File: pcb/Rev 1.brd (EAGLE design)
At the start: 76.8 x 76.8 mm, 216 parts, among them J1 3220-10-0100-00, J2 10118194-0001LF, J3 B2B-PH-K-S(LF)(SN), Q1 MMBT3904,215MMBT3904,215, Q12 MMBT3904,215MMBT3904,215, Q13 MMBT3904,215MMBT3904,215, Q14 MMBT3904,215MMBT3904,215, Q15 MMBT3904,215MMBT3904,215, Q16 TEFT4300, Q17 TEFT4300, Q18 TEFT4300, Q19 TEFT4300, Q20 MMBT3904,215MMBT3904,215, Q21 MMBT3904,215MMBT3904,215, Q22 MMBT3904,215MMBT3904,215, Q23 MMBT3904,215MMBT3904,215, Q24 TEFT4300, Q25 TEFT4300, Q26 TEFT4300, Q27 TEFT4300, Q28 SI7157DP, Q29 SI7157DP, Q30 MMBT3906, Q31 MMBT3906, Q32 SI7157DP, Q33 MMBT3906, Q34 MMBT3906, U1 ATSAMD21G18A-MU, U10 DRV8871, U11 PCAL6416A, U12 MAX7315, U2 AP3441, U3 TPS61089, U4 BNO055, U5 MCP73811, U7 DRV8871, U8 DRV8871, U9 DRV8871

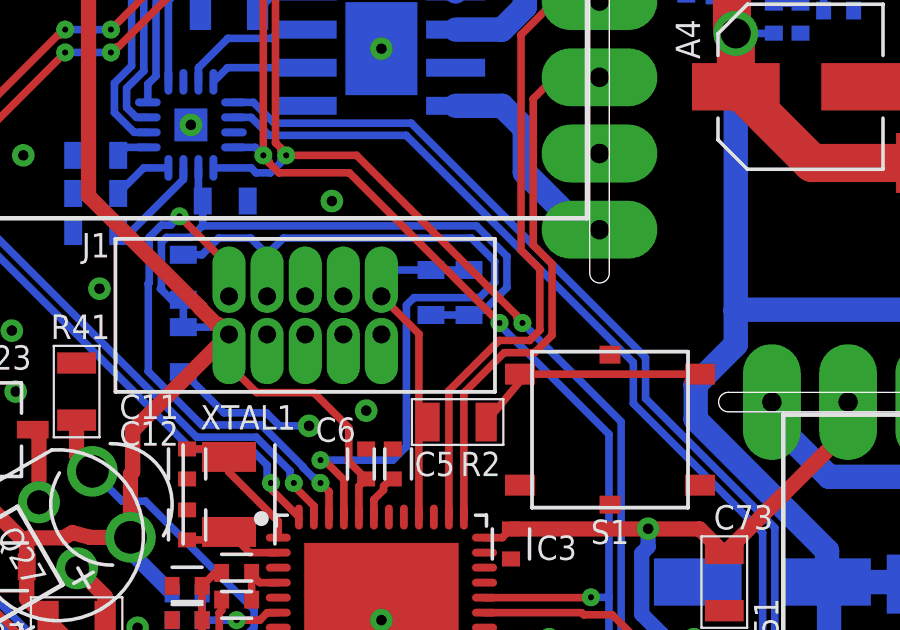
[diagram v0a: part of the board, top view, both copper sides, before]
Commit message: Fixed C7 that was somehow a resistor
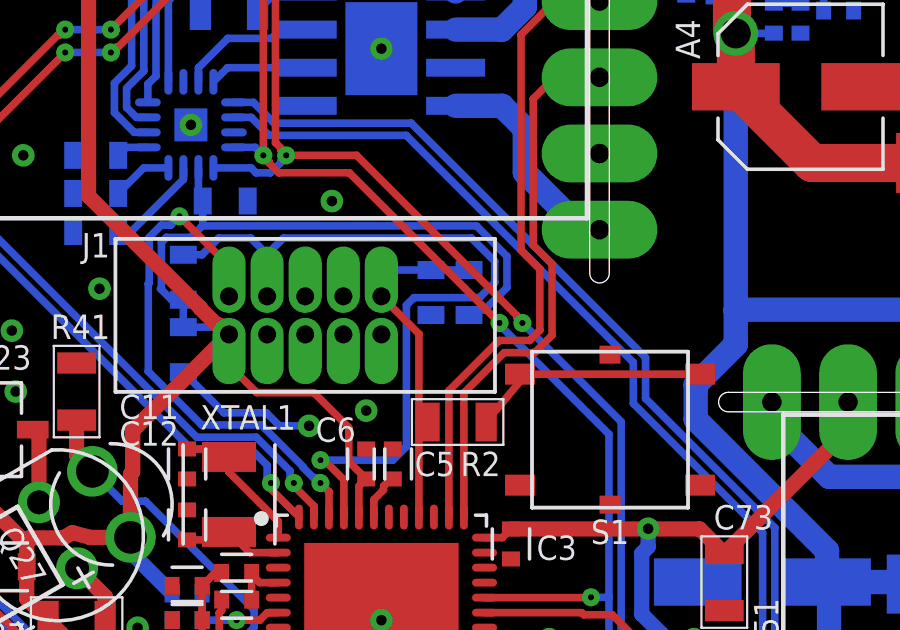
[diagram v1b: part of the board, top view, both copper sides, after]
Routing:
- net +3V3: track 499.9 -> 498.6 mm
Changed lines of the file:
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@@
 <contactref element="FB1" pad="2"/>
 <contactref element="R1" pad="2"/>
-<contactref element="C7" pad="2"/>
 <contactref element="R5" pad="2"/>
 <contactref element="J1" pad="P1"/>
@@
 <wire x1="59.944" y1="20.298" x2="59.944" y2="16.764" width="1.27" layer="16"/>
 <wire x1="59.944" y1="16.764" x2="59.69" y2="16.51" width="1.27" layer="16"/>
-<wire x1="20.701" y1="29.222" x2="21.971" y2="29.222" width="0.254" layer="16"/>
 <wire x1="12.446" y1="28.817" x2="13.728" y2="28.817" width="0.254" layer="16"/>
 <wire x1="13.728" y1="28.817" x2="13.97" y2="28.575" width="0.254" layer="16"/>
@@
 <wire x1="16.8004" y1="26.6336" x2="17.9626" y2="25.4714" width="0.254" layer="1"/>
 <wire x1="17.9626" y1="24.3364" x2="18.542" y2="23.757" width="0.254" layer="1"/>
+<contactref element="C7" pad="2"/>
+<wire x1="22.86" y1="53.492" x2="22.86" y2="55.88" width="0" layer="19" extent="1-1"/>
+<wire x1="20.701" y1="29.222" x2="21.971" y2="29.222" width="0" layer="19" extent="16-16"/>
 </signal>
 <signal name="N$7">

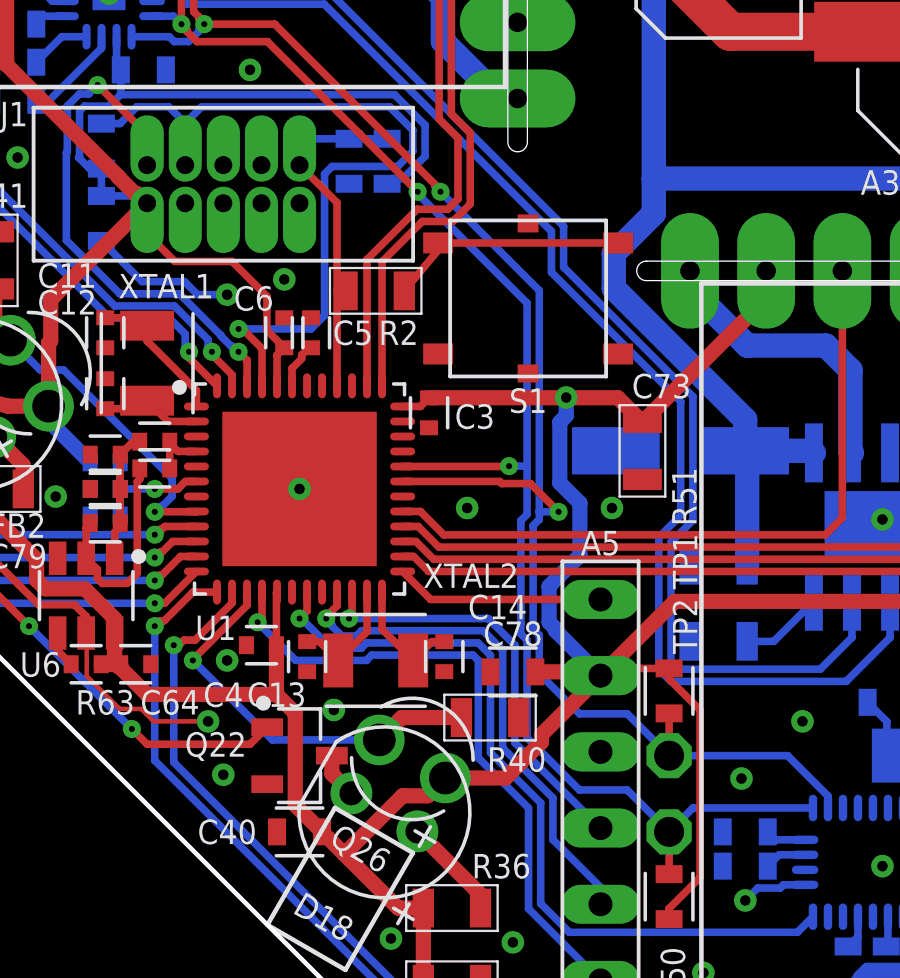
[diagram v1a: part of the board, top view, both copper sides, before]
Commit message: Fixed crystal package
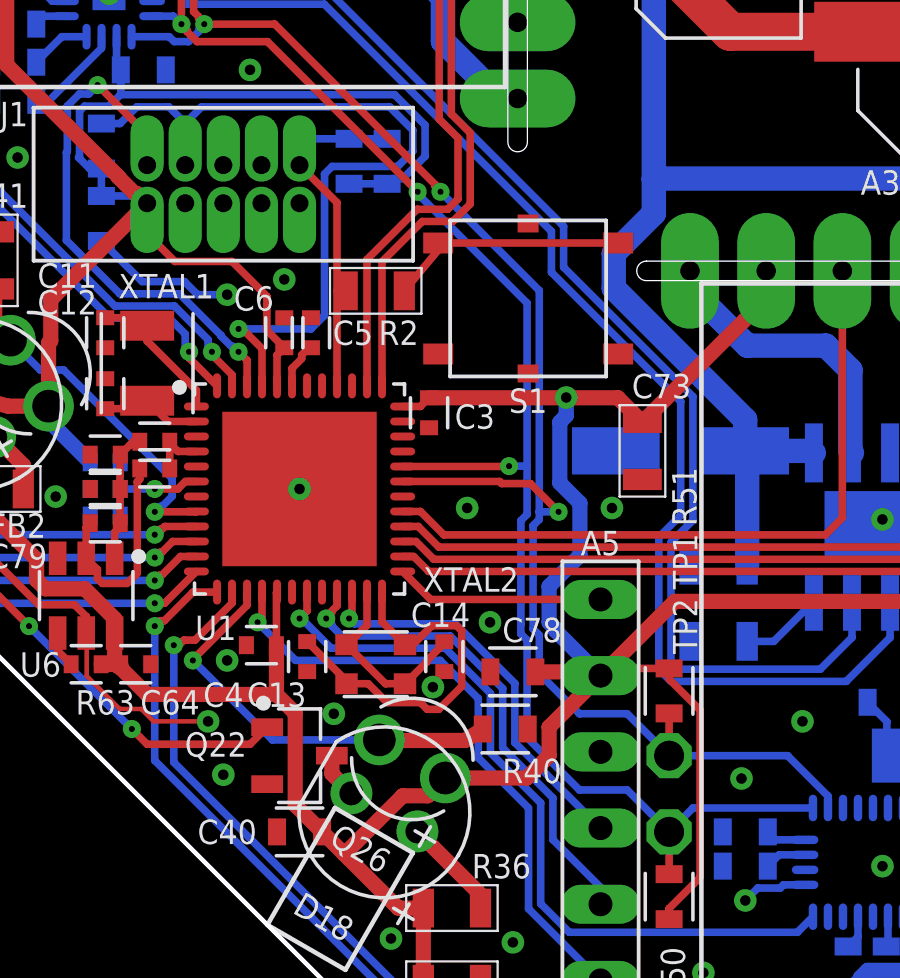
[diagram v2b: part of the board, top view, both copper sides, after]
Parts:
- R40: device Micromouse 2020:0805 -> Micromouse 2020:0603
- XTAL2: device Micromouse 2020:FC-135 -> Micromouse 2020:XRCGB
- moved R40 0.64 mm to (25.9, 11.0)
- moved XTAL2 0.13 mm to (21.6, 13.2)
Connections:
- net GND: now also R40.1; no longer R40.P$1
- net PHOTO7: now also R40.2; no longer R40.P$2
- net XIN: now also C14.2, XTAL2.2, XTAL2.4; no longer C13.2, XTAL2.1
- net XOUT: now also C13.2, XTAL2.1, XTAL2.3; no longer C14.2, XTAL2.2
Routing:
- net XOUT: track 4.00 -> 12.6 mm
- net XIN: track 3.97 -> 6.49 mm
- net +3V3: track 498.6 -> 500.3 mm
- net BT_TX: track 17.4 -> 16.5 mm
- net IMU_INT: track 26.7 -> 25.8 mm
- net BT_STATE: track 21.5 -> 20.6 mm
- net BT_RX: track 14.1 -> 13.4 mm
- net GND: track 36.1 -> 36.7 mm, vias 65 -> 67
- net PHOTO7: track 13.4 -> 13.9 mm

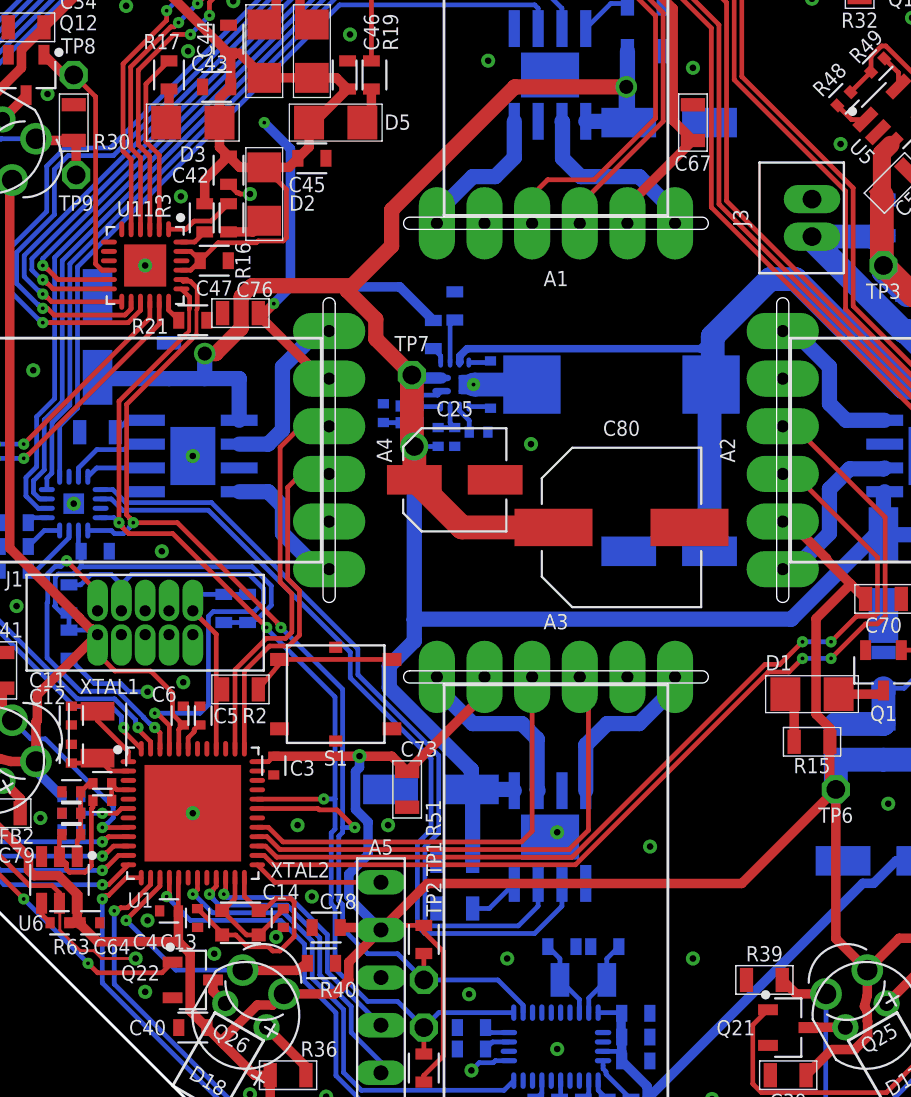
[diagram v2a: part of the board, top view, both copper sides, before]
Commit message: Switched power rail to HC-05
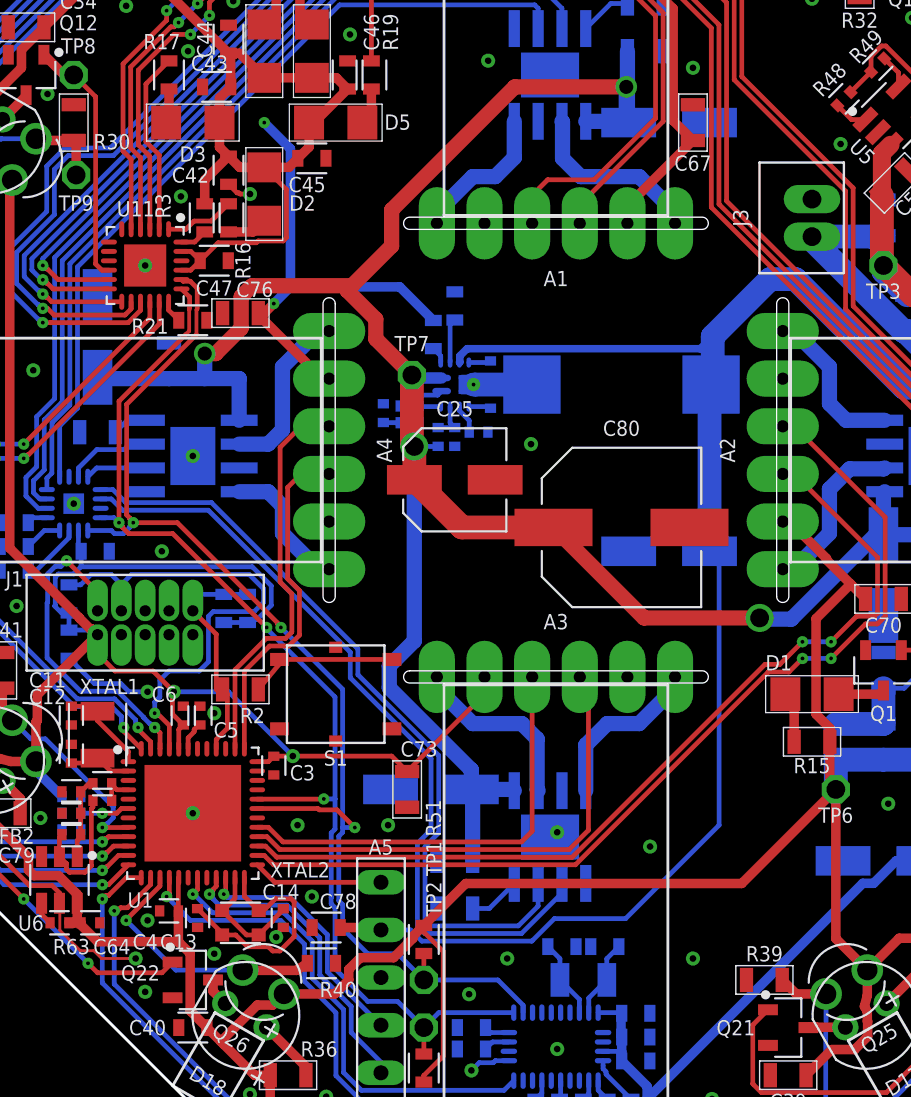
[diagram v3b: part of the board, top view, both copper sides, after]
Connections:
- net +3V3: no longer A5.5, C78.2
- net +3V7: now also A5.5, C78.2
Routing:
- net +3V7: track 145.8 -> 183.7 mm
- net +3V3: track 500.3 -> 492.7 mm, vias 3 -> 4
- net +12V: track 132.7 -> 127.3 mm, vias 3 -> 4

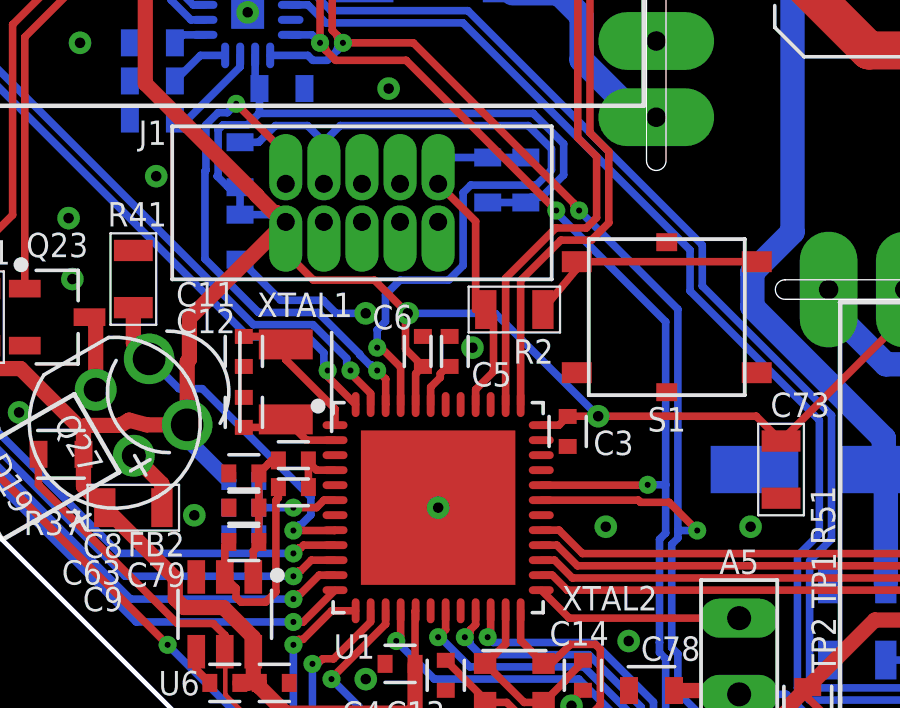
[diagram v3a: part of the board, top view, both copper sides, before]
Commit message: Changed pin mapping
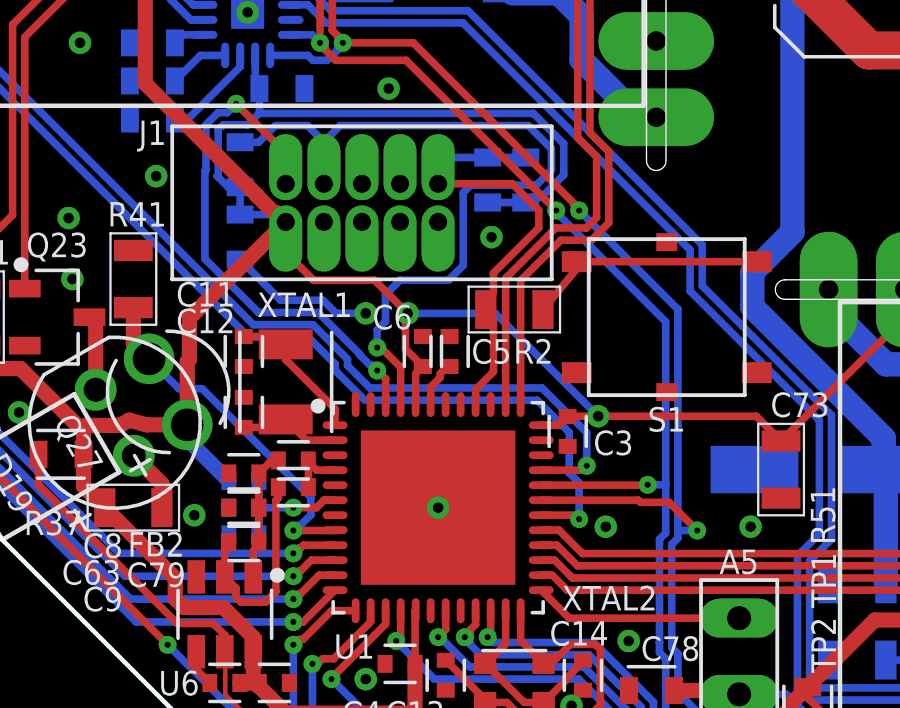
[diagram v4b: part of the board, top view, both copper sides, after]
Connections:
- net ENCODER_1A: now also U1.30; no longer U1.48
- net ENCODER_1B: now also U1.33; no longer U1.47
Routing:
- net ENCODER_1A: track 107.8 -> 119.4 mm
- net ENCODER_1B: track 109.0 -> 119.0 mm
- net !RESET: track 12.3 -> 15.0 mm
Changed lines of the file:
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@@
 </element>
 <element name="C5" library="Micromouse 2020" package="0402" package3d_urn="urn:adsk.eagle:package:16053683/1" value="1uF" x="19.431" y="24.257" smashed="yes" rot="R270">
-<attribute name="NAME" x="20.828" y="23.0886" size="0.8128" layer="25" align="bottom-center"/>
+<attribute name="NAME" x="20.828" y="23.8506" size="0.8128" layer="25" align="bottom-center"/>
 </element>
 <element name="C52" library="Micromouse 2020" package="0603" package3d_urn="urn:adsk.eagle:package:16053670/1" value="0.1uF" x="42.672" y="8.382" smashed="yes" rot="MR0">
@@
 </element>
 <element name="C7" library="Micromouse 2020" package="0603" package3d_urn="urn:adsk.eagle:package:16053670/1" value="100pF" x="20.701" y="29.972" smashed="yes" rot="MR270">
-<attribute name="NAME" x="20.828" y="28.3464" size="0.8128" layer="26" rot="MR180" align="bottom-center"/>
+<attribute name="NAME" x="21.082" y="27.5844" size="0.8128" layer="26" rot="MR180" align="bottom-center"/>
 </element>
 <element name="C70" library="Micromouse 2020" package="0805" value="1uF" x="55.88" y="30.48" smashed="yes" rot="R180">
@@
 <wire x1="23.495" y1="12.581" x2="23.876" y2="12.962" width="0.254" layer="1"/>
 <via x="25.4" y="14.605" extent="1-16" drill="0.35"/>
-<via x="20.193" y="24.384" extent="1-16" drill="0.35"/>
+<via x="20.828" y="28.067" extent="1-16" drill="0.35"/>
 </signal>
 <signal name="N$66">
@@
 <wire x1="19.05" y1="30.607" x2="19.05" y2="29.845" width="0.254" layer="16"/>
 <wire x1="20.3" y1="22.4873" x2="20.3" y2="22.987" width="0.254" layer="1"/>
-<wire x1="20.3" y1="25.654" x2="20.3" y2="28.595" width="0.254" layer="1"/>
-<wire x1="20.3" y1="28.595" x2="19.05" y2="29.845" width="0.254" layer="1"/>
-<wire x1="20.6375" y1="25.654" x2="20.3" y2="25.654" width="0.254" layer="1"/>
 <wire x1="20.3" y1="22.987" x2="20.8936" y2="23.5806" width="0.254" layer="1"/>
 <wire x1="20.8936" y1="25.3979" x2="20.6375" y2="25.654" width="0.254" layer="1"/>
 <wire x1="20.8936" y1="23.5806" x2="20.8936" y2="25.3979" width="0.254" layer="1"/>
+<wire x1="20.6375" y1="25.654" x2="20.6375" y2="25.9715" width="0.254" layer="1"/>
+<wire x1="20.6375" y1="25.9715" x2="20.8936" y2="26.2276" width="0.254" layer="1"/>
+<wire x1="22.4044" y1="28.37900625" x2="22.4044" y2="28.9638625" width="0.254" layer="1"/>
+<wire x1="22.4044" y1="28.9638625" x2="21.5232625" y2="29.845" width="0.254" layer="1"/>
+<wire x1="21.5232625" y1="29.845" x2="19.05" y2="29.845" width="0.254" layer="1"/>
+<wire x1="20.8936" y1="26.2276" x2="20.8936" y2="26.86820625" width="0.254" layer="1"/>
+<wire x1="20.8936" y1="26.86820625" x2="22.4044" y2="28.37900625" width="0.254" layer="1"/>
 </signal>
 <signal name="N$4">
@@
 <wire x1="3.048" y1="44.896075" x2="3.048" y2="43.434" width="0.254" layer="1"/>
 <wire x1="2.4654" y1="45.478675" x2="3.048" y2="44.896075" width="0.254" layer="1"/>
-<via x="15.367" y="23.622" extent="1-16" drill="0.2"/>
-<contactref element="U1" pad="48"/>
-<wire x1="16.3" y1="22.4873" x2="15.367" y2="23.4203" width="0.254" layer="1"/>
-<wire x1="15.367" y1="23.4203" x2="15.367" y2="23.622" width="0.254" layer="1"/>
-<wire x1="15.367" y1="23.622" x2="15.24" y2="23.749" width="0.254" layer="16"/>
-<wire x1="15.24" y1="23.749" x2="15.24" y2="24.214125" width="0.254" layer="16"/>
 <wire x1="2.8448" y1="43.2308" x2="3.048" y2="43.434" width="0.254" layer="16"/>
-<wire x1="15.24" y1="24.214125" x2="14.7105625" y2="24.7435625" width="0.254" layer="16"/>
 <wire x1="12.72483125" y1="24.7435625" x2="2.8448" y2="34.62359375" width="0.254" layer="16"/>
 <wire x1="2.8448" y1="34.62359375" x2="2.8448" y2="43.2308" width="0.254" layer="16"/>
 <wire x1="12.72483125" y1="24.7435625" x2="14.7105625" y2="24.7435625" width="0.254" layer="16"/>
+<via x="23.749" y="18.669" extent="1-16" drill="0.2"/>
+<contactref element="U1" pad="30"/>
+<wire x1="23.749" y1="18.669" x2="23.618" y2="18.8" width="0.254" layer="1"/>
+<wire x1="23.618" y1="18.8" x2="22.4873" y2="18.8" width="0.254" layer="1"/>
+<wire x1="15.6226" y1="23.831525" x2="15.6226" y2="23.6187375" width="0.254" layer="16"/>
+<wire x1="15.6226" y1="23.6187375" x2="16.6083375" y2="22.633" width="0.254" layer="16"/>
+<wire x1="23.4204" y1="20.205675" x2="23.749" y2="19.877075" width="0.254" layer="16"/>
+<wire x1="23.749" y1="19.877075" x2="23.749" y2="18.669" width="0.254" layer="16"/>
+<wire x1="23.4204" y1="21.556875" x2="23.4204" y2="20.205675" width="0.254" layer="16"/>
+<wire x1="14.7105625" y1="24.7435625" x2="15.6226" y2="23.831525" width="0.254" layer="16"/>
+<wire x1="16.6083375" y1="22.633" x2="22.344275" y2="22.633" width="0.254" layer="16"/>
+<wire x1="22.344275" y1="22.633" x2="23.4204" y2="21.556875" width="0.254" layer="16"/>
 </signal>
 <signal name="ENCODER_1B">
@@
 <wire x1="3.048" y1="45.72" x2="3.81" y2="44.958" width="0.254" layer="1"/>
 <wire x1="3.81" y1="44.958" x2="3.81" y2="43.434" width="0.254" layer="1"/>
-<via x="16.129" y="23.622" extent="1-16" drill="0.2"/>
-<contactref element="U1" pad="47"/>
-<wire x1="16.129" y1="23.622" x2="16.129" y2="23.52675625" width="0.254" layer="1"/>
-<wire x1="16.8" y1="22.85575625" x2="16.8" y2="22.4873" width="0.254" layer="1"/>
-<wire x1="16.129" y1="23.52675625" x2="16.8" y2="22.85575625" width="0.254" layer="1"/>
-<wire x1="16.129" y1="23.622" x2="16.002" y2="23.749" width="0.254" layer="16"/>
-<wire x1="16.002" y1="24.0268625" x2="16.002" y2="23.749" width="0.254" layer="16"/>
 <wire x1="3.6306" y1="43.192675" x2="3.6306" y2="43.2546" width="0.254" layer="16"/>
 <wire x1="3.6306" y1="43.2546" x2="3.81" y2="43.434" width="0.254" layer="16"/>
@@
 <wire x1="3.2512" y1="42.813275" x2="3.2512" y2="34.79193125" width="0.254" layer="16"/>
 <wire x1="12.89316875" y1="25.1499625" x2="14.8789" y2="25.1499625" width="0.254" layer="16"/>
-<wire x1="14.8789" y1="25.1499625" x2="16.002" y2="24.0268625" width="0.254" layer="16"/>
 <wire x1="3.2512" y1="34.79193125" x2="12.89316875" y2="25.1499625" width="0.254" layer="16"/>
+<wire x1="16.029" y1="23.9998625" x2="16.029" y2="23.787075" width="0.254" layer="16"/>
+<wire x1="16.029" y1="23.787075" x2="16.776675" y2="23.0394" width="0.254" layer="16"/>
+<wire x1="14.8789" y1="25.1499625" x2="16.029" y2="23.9998625" width="0.254" layer="16"/>
+<wire x1="16.776675" y1="23.0394" x2="22.5126125" y2="23.0394" width="0.254" layer="16"/>
+<via x="24.003" y="20.447" extent="1-16" drill="0.2"/>
+<contactref element="U1" pad="33"/>
+<wire x1="24.003" y1="20.447" x2="23.856" y2="20.3" width="0.254" layer="1"/>
+<wire x1="23.856" y1="20.3" x2="22.4873" y2="20.3" width="0.254" layer="1"/>
+<wire x1="24.003" y1="21.5490125" x2="24.003" y2="20.447" width="0.254" layer="16"/>
+<wire x1="22.5126125" y1="23.0394" x2="24.003" y2="21.5490125" width="0.254" layer="16"/>
 </signal>
 <signal name="N$85">
